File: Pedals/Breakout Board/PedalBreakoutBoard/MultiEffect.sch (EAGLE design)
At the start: 69 parts, among them IC1 LD1117V, IC2 MCP6004P, U1 OPA1652AID

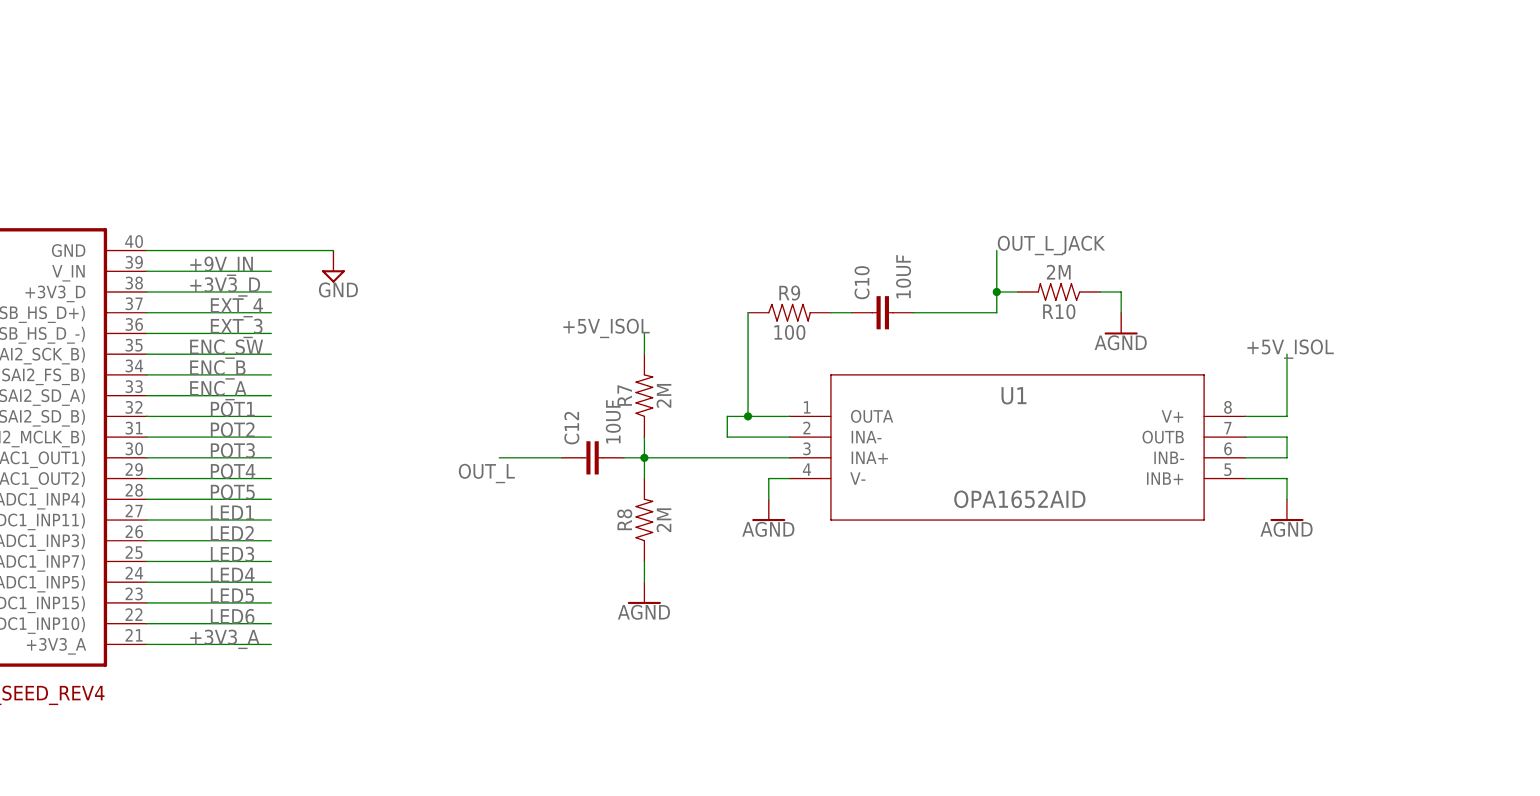
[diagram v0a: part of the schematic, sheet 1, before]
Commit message: DP-97 - Add power conditioning caps to 3V3_D
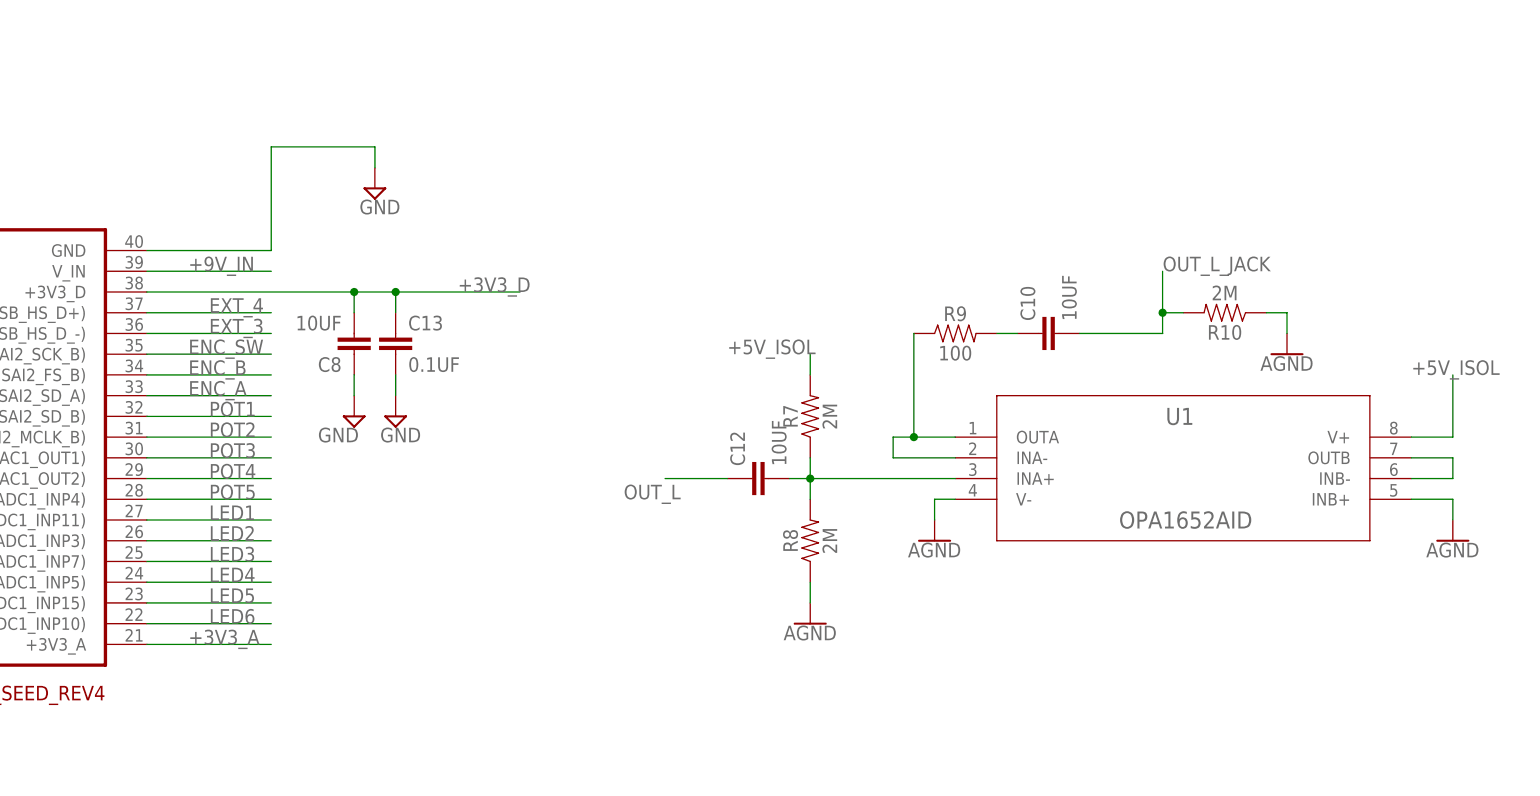
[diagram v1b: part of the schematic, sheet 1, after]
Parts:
- added C13: 0.1UF, Custom-Parts:0.1UF
- added C8: 10UF, Custom-Parts:10UF
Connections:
- net +3V3_D: now also C13.1, C8.2
- net GND: now also C13.2, C8.1
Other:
- moved on the sheet: C10, C12, R10, R7, R8, R9, U1
